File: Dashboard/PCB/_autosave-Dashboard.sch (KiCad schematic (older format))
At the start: 114 parts, among them J1 Display, J2 34912-6080, J3 Conn_01x04_Female, J7 PROGRAMMER, P1 USB_C_Plug, Q1 Q_NMOS_GDS, SW1 SW_SPST, U1 STM32F767ZIT6, U10 24LC01, U2 IFX27001TFV33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

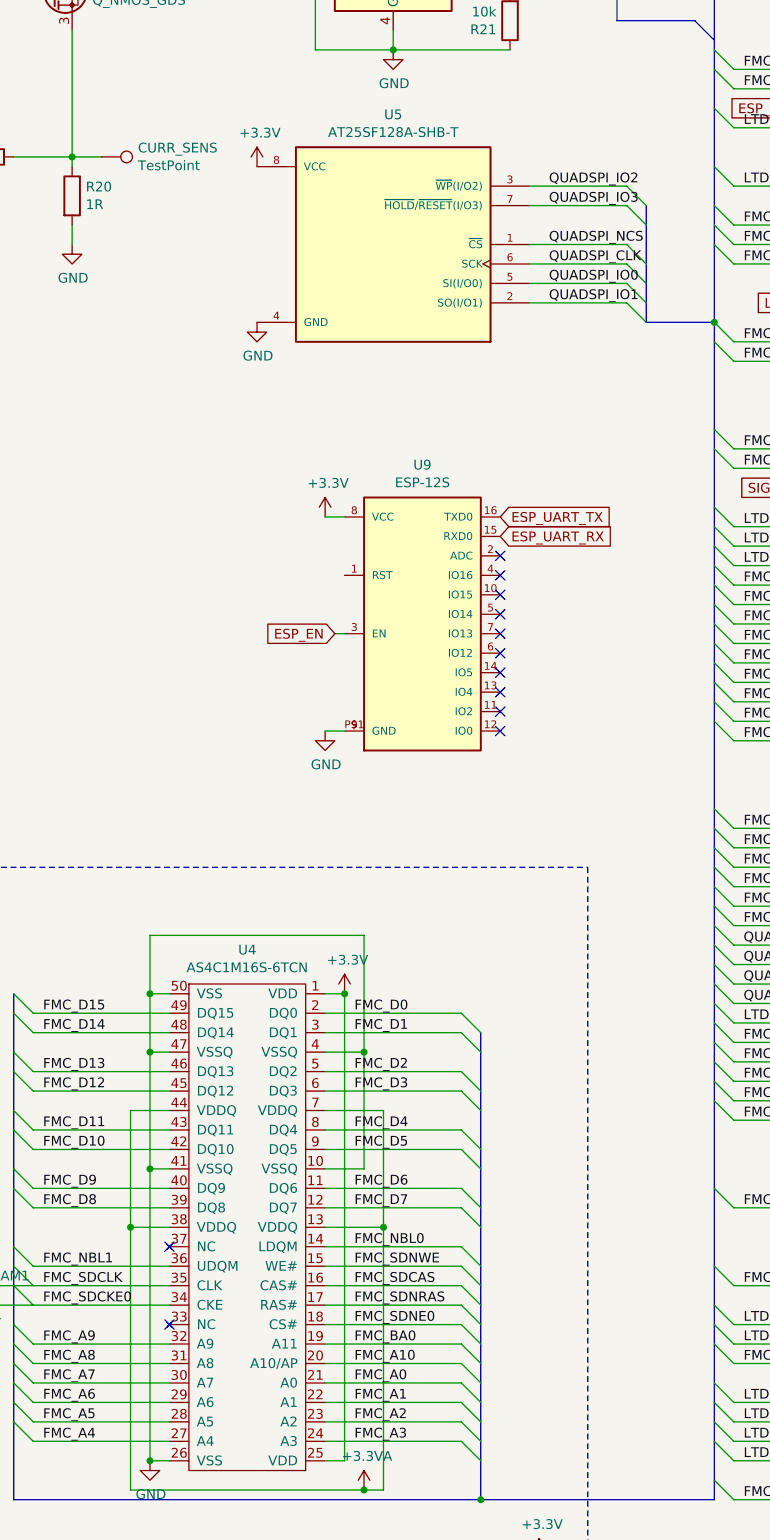
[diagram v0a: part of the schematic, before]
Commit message: Add new PCB for Dashboard (#34)
* Add usb C to board

* Add reset and pd pin to esp

* Switch footprints of converter

* Add LED Driver

* Add text to pcb

* New PCB for Dashboard
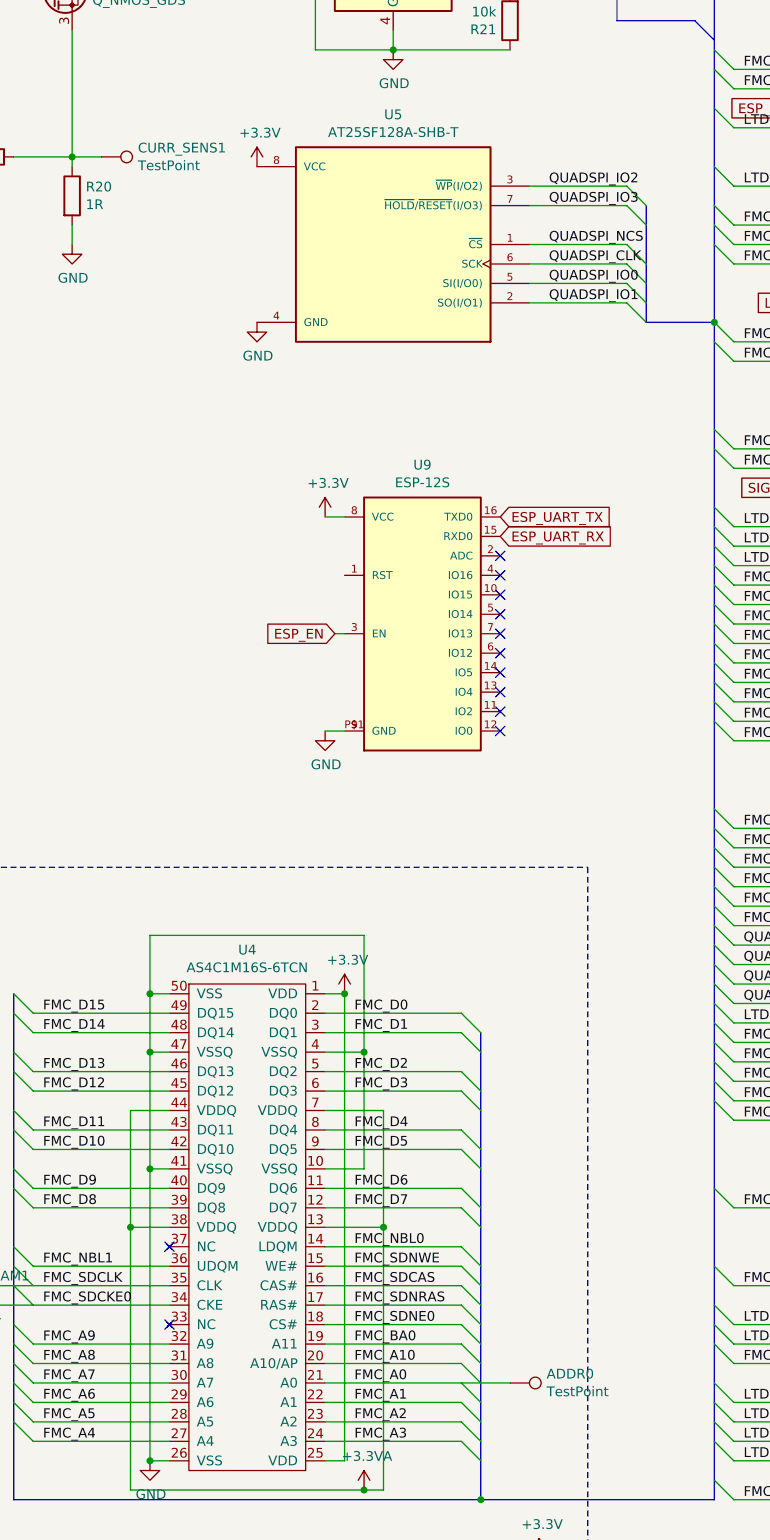
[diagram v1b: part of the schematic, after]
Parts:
- added ADDR0: TestPoint, symbol Connector:TestPoint
- renumbered CURR_SENS to CURR_SENS1
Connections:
- net FMC_A0: now also ADDR0.1
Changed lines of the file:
@@
 	13250 13500 12550 13500
 Wire Wire Line
-	12550 13400 13250 13400
-Wire Wire Line
 	13250 13300 12550 13300
 Wire Wire Line
@@
 Connection ~ 11250 7100
 $Comp
-L Connector:TestPoint CURR_SENS
+L Connector:TestPoint CURR_SENS1
 U 1 1 63718E8A
 P 11400 7100
-F 0 "CURR_SENS" V 11354 7288 50  0000 L CNN
+F 0 "CURR_SENS1" V 11354 7288 50  0000 L CNN
 F 1 "TestPoint" V 11445 7288 50  0000 L CNN
 F 2 "TestPoint:TestPoint_Pad_D1.0mm" H 11600 7100 50  0001 C CNN
@@
 Wire Wire Line
 	10800 13000 11750 13000
-Wire Bus Line
-	14050 6050 14050 6400
-Wire Wire Line
-	12300 4350 13150 4350
-Wire Wire Line
-	12300 4450 13150 4450
-Wire Wire Line
-	12300 4550 13150 4550
-Wire Wire Line
-	12300 4150 13150 4150
-Wire Bus Line
-	13050 1650 13050 5450
-Wire Bus Line
-	14200 7350 14200 7950
-Wire Bus Line
-	14550 800  14550 7950
-Wire Wire Line
-	10850 12900 11750 12900
-Wire Bus Line
-	10950 11400 10950 14000
-Wire Bus Line
-	13350 11600 13350 14000
-Wire Bus Line
-	14550 7950 14550 14000
 $Comp
 L Connector:TestPoint CAN_L1
@@
 	0    1    1    0
 $EndComp
+$Comp
+L Connector:TestPoint ADDR0
+U 1 1 66A90D58
+P 13500 13400
+F 0 "ADDR0" V 13454 13588 50  0000 L CNN
+F 1 "TestPoint" V 13545 13588 50  0000 L CNN
+F 2 "" H 13700 13400 50  0001 C CNN
+F 3 "~" H 13700 13400 50  0001 C CNN
+	1    13500 13400
+	0    1    1    0
+$EndComp
+Wire Wire Line
+	12300 4350 13150 4350
+Wire Wire Line
+	12300 4450 13150 4450
+Wire Wire Line
+	12300 4550 13150 4550
+Wire Wire Line
+	12300 4150 13150 4150
+Wire Wire Line
+	10850 12900 11750 12900
+Wire Wire Line
+	12550 13400 13500 13400
+Wire Bus Line
+	14050 6050 14050 6400
+Wire Bus Line
+	14200 7350 14200 7950
+Wire Bus Line
+	10950 11400 10950 14000
+Wire Bus Line
+	13350 11600 13350 14000
+Wire Bus Line
+	13050 1650 13050 5450
+Wire Bus Line
+	14550 800  14550 7950
+Wire Bus Line
+	14550 7950 14550 14000
 $EndSCHEMATC
